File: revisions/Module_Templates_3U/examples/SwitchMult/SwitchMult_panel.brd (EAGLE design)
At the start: 128.5 x 20 mm, 0 parts

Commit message: Update Backplane Reference
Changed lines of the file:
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@@
 <wire x1="128.5" y1="0" x2="128.5" y2="20" width="0" layer="20"/>
 <wire x1="128.5" y1="20" x2="0" y2="20" width="0" layer="20"/>
-<hole x="52" y="5" drill="7.5"/>
+<hole x="52" y="5" drill="6"/>
 <hole x="66" y="5" drill="7.5"/>
 <hole x="80" y="5" drill="7.5"/>

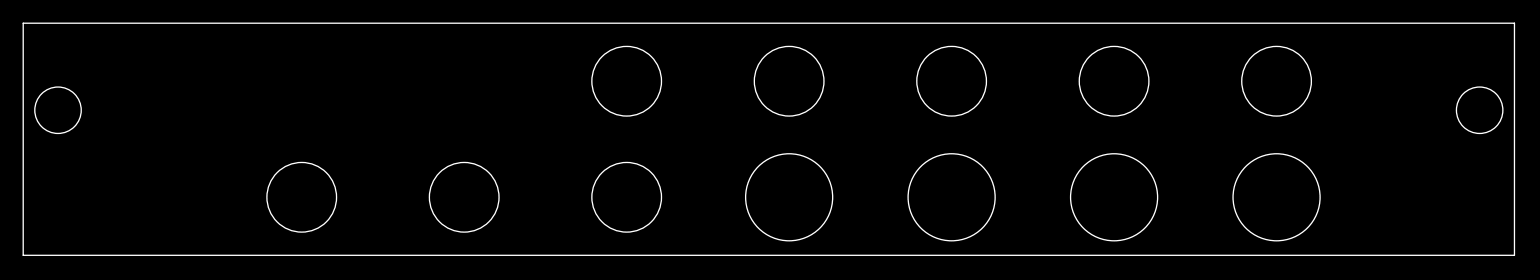
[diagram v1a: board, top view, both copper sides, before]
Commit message: Enlarge SwitchMult Front panel holes for easier assembly/operation
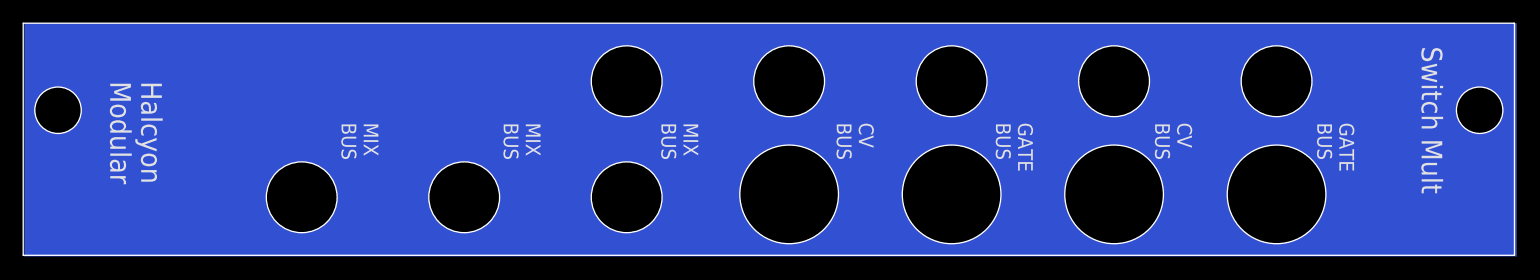
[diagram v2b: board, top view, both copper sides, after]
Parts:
- added U$1: PA_LOGO_SYMLARGE, PatternAgents-Logos:PA_LOGO_AGENT_LRG_SYM
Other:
- board text added: "CV BUS"
- board text added: "GATE BUS"
- board text added: "Halcyon Modular"
- board text added: "MIX BUS"
- board text added: "PatternAgents"
- board text added: "Switch Mult"
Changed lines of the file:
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@@
 <setting verticaltext="up"/>
 </settings>
-<grid distance="0.1" unitdist="mm" unit="mm" style="lines" multiple="1" display="yes" altdistance="0.025" altunitdist="inch" altunit="inch"/>
+<grid distance="1" unitdist="mm" unit="mm" style="lines" multiple="1" display="yes" altdistance="0.025" altunitdist="inch" altunit="inch"/>
 <layers>
 <layer number="1" name="Top" color="4" fill="1" visible="yes" active="yes"/>
@@
 <layer number="24" name="bOrigins" color="15" fill="1" visible="yes" active="yes"/>
 <layer number="25" name="tNames" color="7" fill="1" visible="yes" active="yes"/>
-<layer number="26" name="bNames" color="7" fill="1" visible="yes" active="yes"/>
+<layer number="26" name="bNames" color="7" fill="1" visible="no" active="yes"/>
 <layer number="27" name="tValues" color="7" fill="1" visible="no" active="yes"/>
 <layer number="28" name="bValues" color="7" fill="1" visible="no" active="yes"/>
@@
 <wire x1="128.5" y1="0" x2="128.5" y2="20" width="0" layer="20"/>
 <wire x1="128.5" y1="20" x2="0" y2="20" width="0" layer="20"/>
-<hole x="52" y="5" drill="6"/>
-<hole x="66" y="5" drill="7.5"/>
-<hole x="80" y="5" drill="7.5"/>
-<hole x="94" y="5" drill="7.5"/>
-<hole x="108" y="5" drill="7.5"/>
-<hole x="66" y="15" drill="6"/>
-<hole x="52" y="15" drill="6"/>
-<hole x="38" y="5" drill="6"/>
-<hole x="24" y="5" drill="6"/>
-<hole x="80" y="15" drill="6"/>
-<hole x="94" y="15" drill="6"/>
-<hole x="108" y="15" drill="6"/>
+<hole x="52" y="5" drill="6.1"/>
+<hole x="66" y="5.25" drill="8.5"/>
+<hole x="80" y="5.25" drill="8.5"/>
+<hole x="94" y="5.25" drill="8.5"/>
+<hole x="108" y="5.25" drill="8.5"/>
+<hole x="66" y="15" drill="6.1"/>
+<hole x="52" y="15" drill="6.1"/>
+<hole x="38" y="5" drill="6.1"/>
+<hole x="24" y="5" drill="6.1"/>
+<hole x="80" y="15" drill="6.1"/>
+<hole x="94" y="15" drill="6.1"/>
+<hole x="108" y="15" drill="6.1"/>
 <hole x="3" y="12.5" drill="4"/>
 <hole x="125.5" y="12.5" drill="4"/>
+<rectangle x1="0.1" y1="-0.1" x2="128.7" y2="20" layer="16"/>
+<text x="111.506" y="11.43" size="1.27" layer="21" font="vector" ratio="24" rot="SR270">GATE
+BUS</text>
+<text x="83.82" y="11.43" size="1.27" layer="21" font="vector" ratio="24" rot="SR270">GATE
+BUS</text>
+<text x="97.536" y="11.43" size="1.27" layer="21" font="vector" ratio="24" rot="SR270">CV
+BUS</text>
+<text x="70.104" y="11.43" size="1.27" layer="21" font="vector" ratio="24" rot="SR270">CV
+BUS</text>
+<text x="54.991" y="11.43" size="1.27" layer="21" font="vector" ratio="24" rot="SR270">MIX
+BUS</text>
+<text x="27.432" y="11.43" size="1.27" layer="21" font="vector" ratio="24" rot="SR270">MIX
+BUS</text>
+<text x="41.402" y="11.43" size="1.27" layer="21" font="vector" ratio="24" rot="SR270">MIX
+BUS</text>
+<text x="120.5" y="18" size="1.778" layer="21" font="vector" ratio="24" rot="SR270">Switch Mult</text>
+<text x="6.604" y="0.998" size="1.6764" layer="22" font="vector" ratio="20" rot="SMR90">PatternAgents</text>
+<text x="7.5" y="15" size="1.778" layer="21" font="vector" ratio="24" rot="SR270">Halcyon
+Modular</text>
 </plain>
 <attributes>
@@
 </autorouter>
 <elements>
+<element name="U$1" library="PatternAgents-Logos" package="PA_LOGO_AGENT_LRG_SYM" value="PA_LOGO_SYMLARGE" x="12.7" y="10.16" rot="MR90"/>
 </elements>
 <signals>
@@
 </board>
 </drawing>
+<compatibility>
+<note version="6.3" minversion="6.2.2" severity="warning">
+Since Version 6.2.2 text objects can contain more than one line,
+which will not be processed correctly with this version.
+</note>
+</compatibility>
 </eagle>
